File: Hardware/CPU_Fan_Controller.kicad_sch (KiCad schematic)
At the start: 15 parts, among them J1 Conn_01x05_Pin, J3 Conn_01x01_Socket, J4 Conn_01x01_Socket, M1 Fan_CPU_4pin, SW1 SW_Push, U1 STM32G030J6Mx, U2 LT1962-3.3

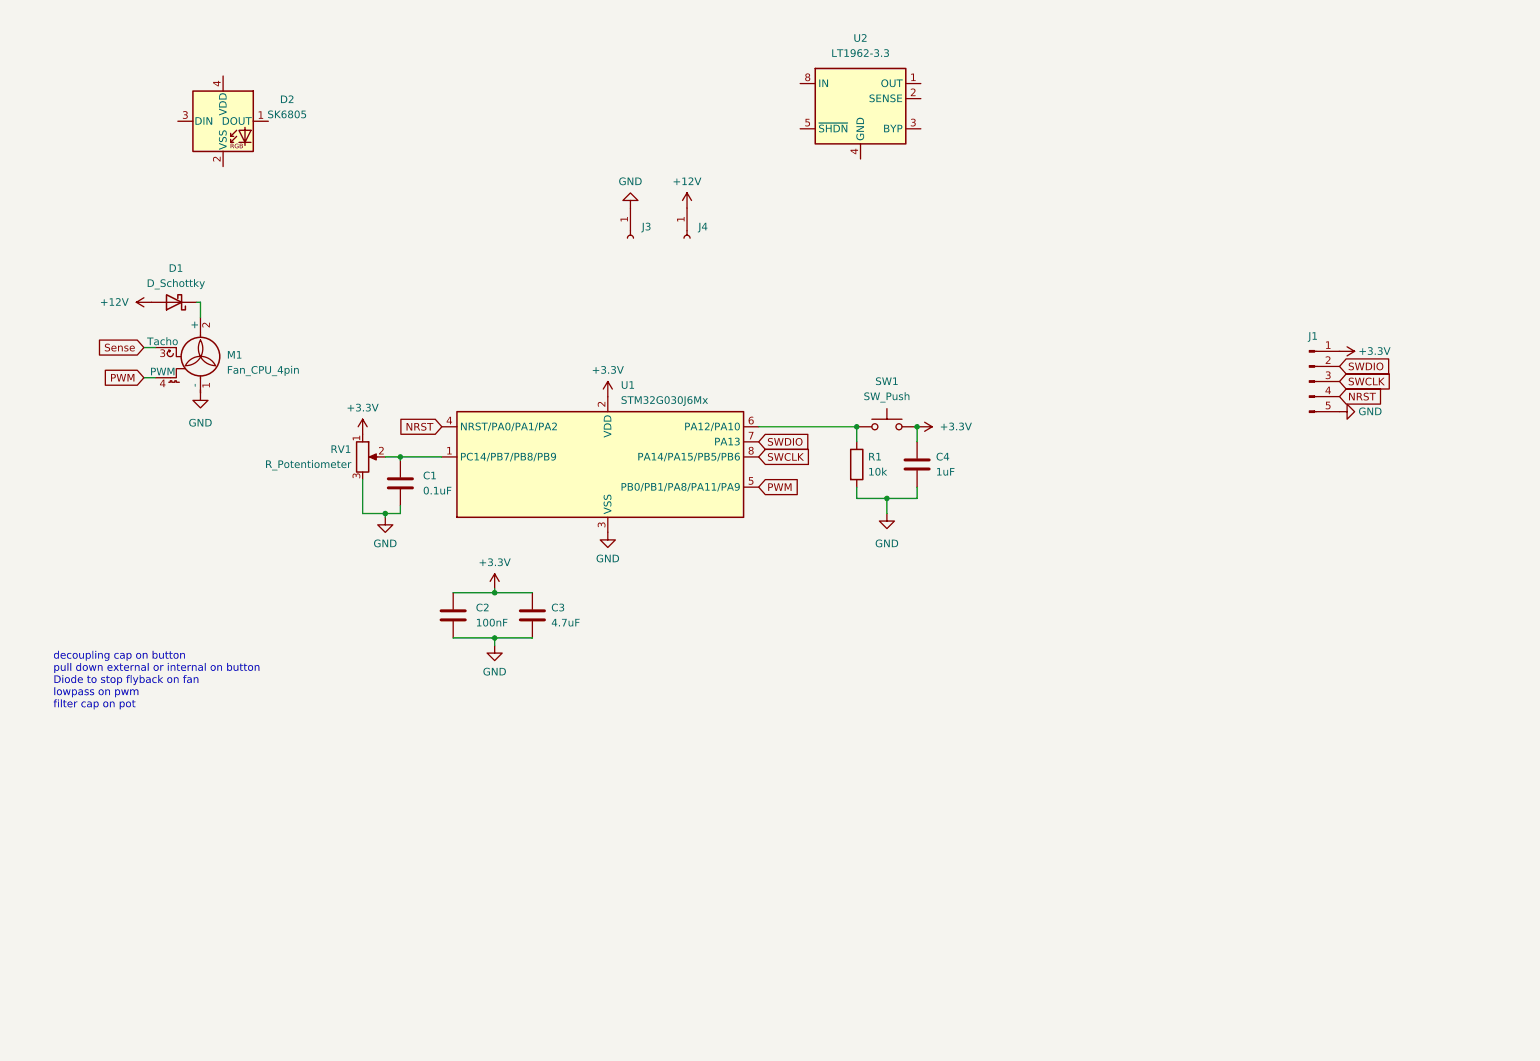
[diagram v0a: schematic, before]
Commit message: Code is functioning, updated PCB
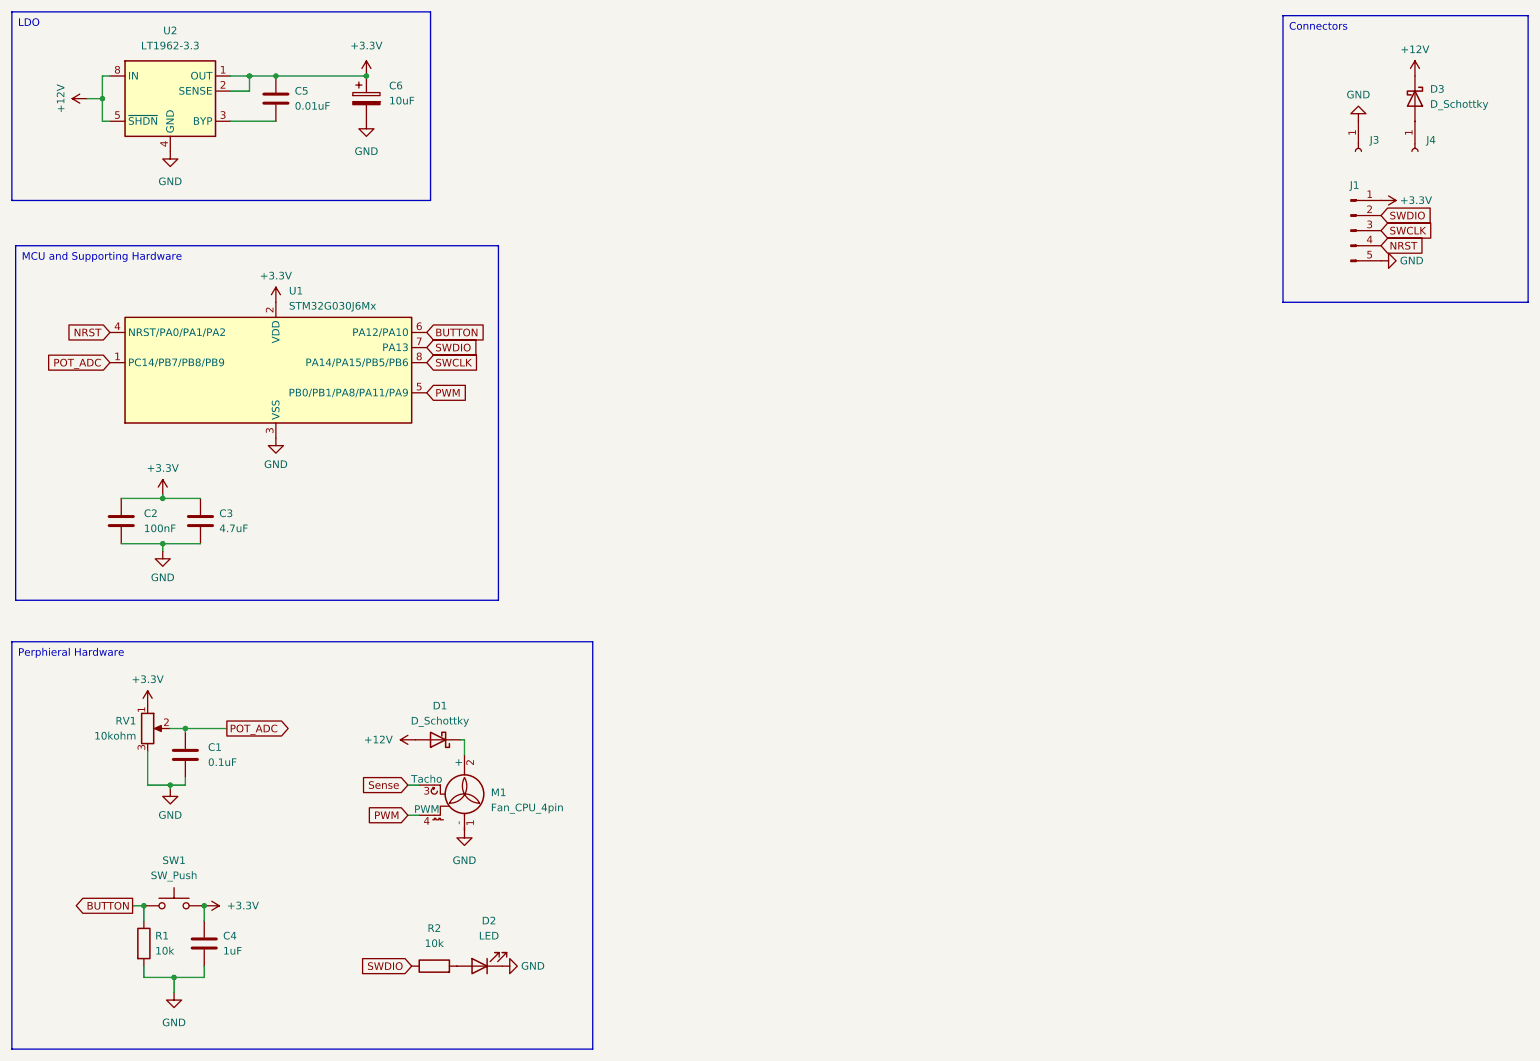
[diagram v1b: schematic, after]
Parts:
- removed D2: SK6805, LED_SMD:LED_SK6812_EC15_1.5x1.5mm, symbol LED:SK6805
- added C5: 0.01uF, Capacitor_SMD:C_0603_1608Metric_Pad1.08x0.95mm_HandSolder, symbol Device:C
- added C6: 10uF, Capacitor_Tantalum_SMD:CP_EIA-6032-15_Kemet-U, symbol Device:C_Polarized
- added D2: LED, LED_SMD:LED_0603_1608Metric, symbol Device:LED
- added D3: D_Schottky, Diode_SMD:D_0805_2012Metric_Pad1.15x1.40mm_HandSolder, symbol Device:D_Schottky
- added R2: 10k, Resistor_SMD:R_0603_1608Metric_Pad0.98x0.95mm_HandSolder, symbol Device:R
- C4: footprint (none) -> Capacitor_SMD:C_0603_1608Metric_Pad1.08x0.95mm_HandSolder
- D1: footprint Diode_SMD:D_0603_1608Metric -> Diode_SMD:D_0805_2012Metric_Pad1.15x1.40mm_HandSolder
- M1: footprint (none) -> Connector_PinHeader_2.54mm:PinHeader_1x04_P2.54mm_Horizontal
- R1: footprint (none) -> Resistor_SMD:R_0603_1608Metric_Pad0.98x0.95mm_HandSolder
- RV1: value R_Potentiometer -> 10kohm
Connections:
- net +12V: now also U2.5 (~{SHDN}), U2.8 (IN), D3.1 (K); no longer J4.1 (Pin_1)
- net +3.3V: now also U2.1 (OUT), U2.2 (SENSE), C5.2, C6.1
- net GND: now also U2.4 (GND), C6.2, D2.1 (K)
- net SWDIO: now also R2.1
- net POT_ADC: now reaches C1.1, RV1.2, U1.1 (PC14/PB7/PB8/PB9)
- net at U2.3 (BYP): now also C5.1
- net BUTTON: now reaches R1.1, SW1.1, U1.6 (PA12/PA10)
- new net: D3.2 (A), J4.1 (Pin_1)
- new net: D2.2 (A), R2.2
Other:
- note removed: "decoupling cap on button pull down external or internal on button Diode to stop flyback on fan lowpass on pwm filter cap on pot"
- moved on the sheet: C2, C3, D1, J1, J3, J4, M1, U1, U2
